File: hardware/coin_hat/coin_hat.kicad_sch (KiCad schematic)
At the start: 56 parts, among them J1 Pi 40-pin (bottom side), J10 Coin sensor, J11 Aux header, J12 Aux 12V switched, J2 Belt motor, J3 Feeder motor, J4 Diverter servo (1 SIG / 2 V+ 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, J5 12 V in 5.5/2.1, J6 LED ring (WS2812), J7 Key light 12V switched, J9 Home: feeder, Q1 AO3400, Q2 AO3400, Q3 AO3400, U1 Raspberry Pi Pico, U2 StepStick (TMC2209 or A4988), U3 StepStick (TMC2209 or A4988), U5 12V->5V 5A module (Pololu D24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, U6 74AHCT1G125, U7 CAT24C32, U8 12V->5-6V 3A servo buck (Polo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

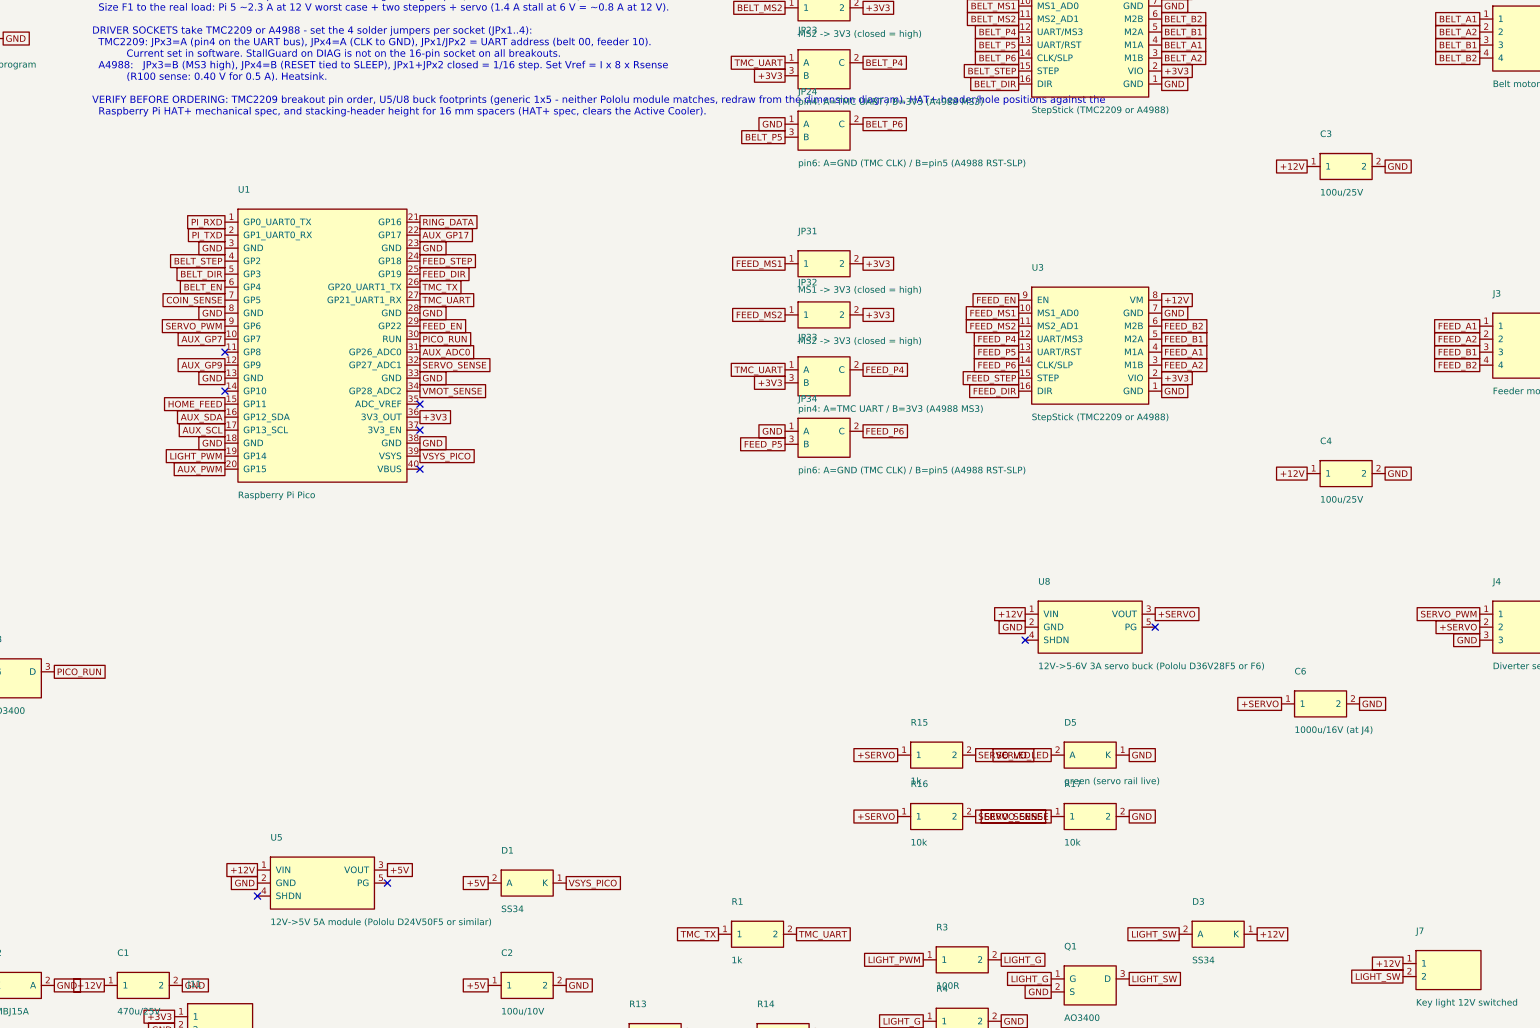
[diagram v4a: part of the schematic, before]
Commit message: coin_hat: draw Pololu buck footprints from the drill guides
U5 and U8 were a generic 1x5 header that matched neither module. Add a
project footprint library (coin_hat.pretty + fp-lib-table) with
Pololu_D24V50F5 and Pololu_D36V28Fx, placing pads and #2 mounting holes
at the coordinates in Pololu's drill-guide DXFs (reg15d01, reg24g), top
view, pad 1 = EN:

  D24V50F5  EN VIN GND GND VOUT
  D36V28Fx  EN VIN GND GND VOUT, PG 0.1" inboard of EN

Replace the generic Buck symbol with one symbol per module. EN is left
open (100k pull-up to VIN on both modules) and PG is unused. ERC is
clean, every pin maps to a pad, and the floor plan still packs with the
real 18.4 x 20.9 courtyards.

Co-Authored-By: Claude Opus 5.5 <noreply@anthropic.com>
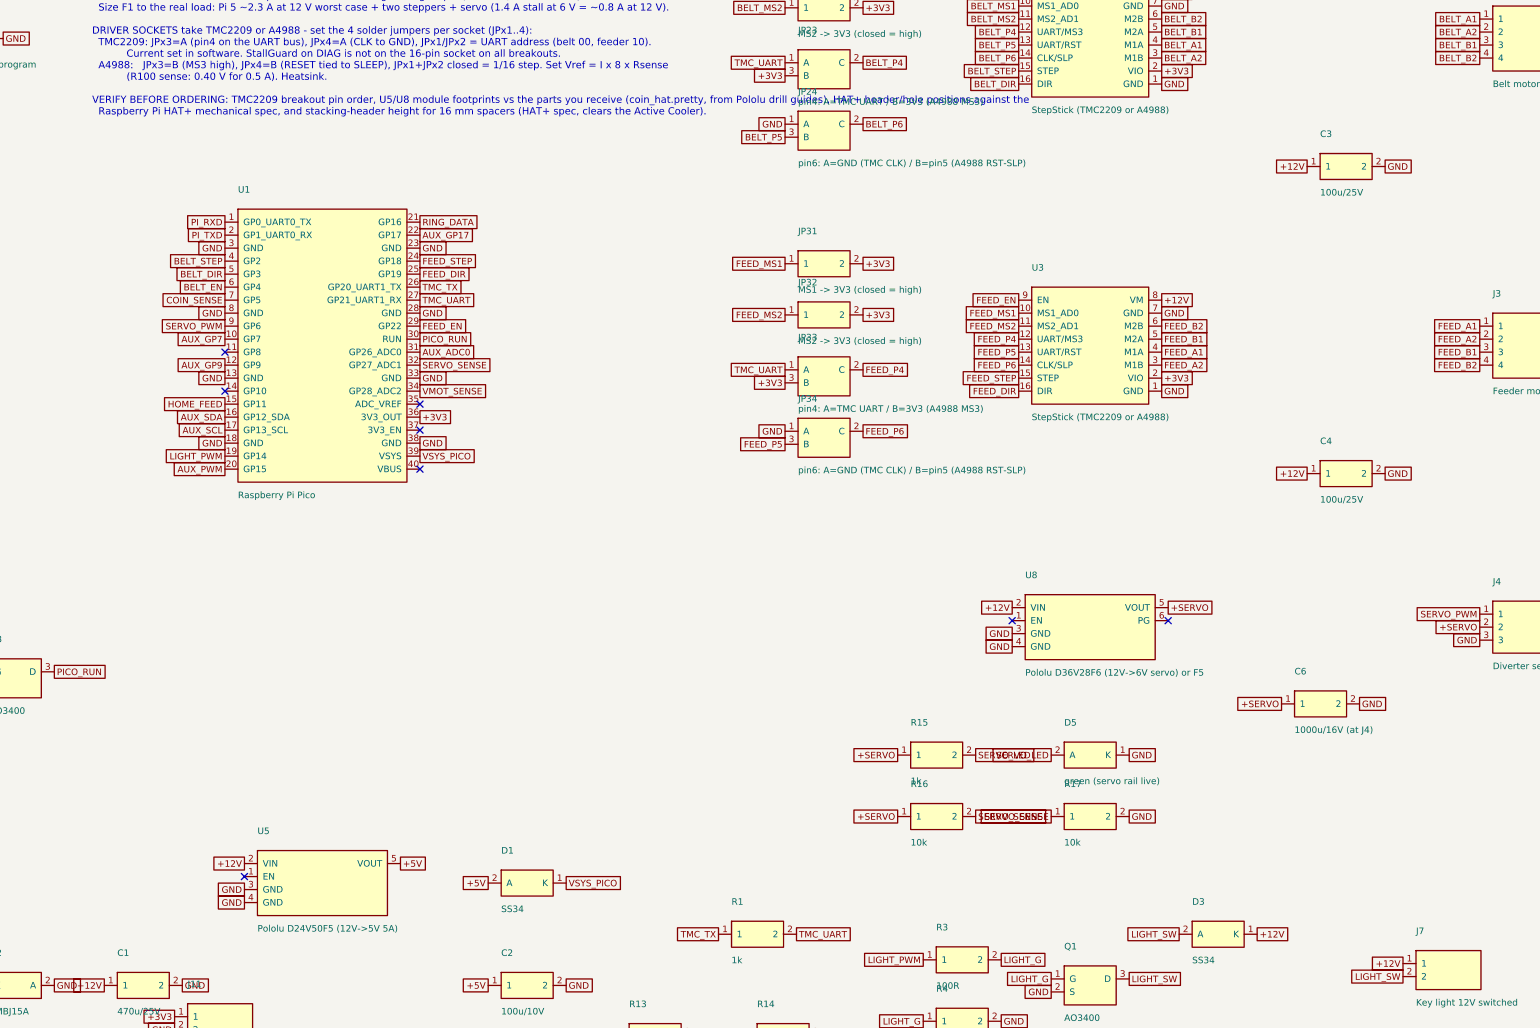
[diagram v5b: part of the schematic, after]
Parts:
- removed U5: 12V->5V 5A module (Pololu D24V50F5 or similar), Connector_PinHeader_2.54mm:PinHeader_1x05_P2.54mm_Vertical, symbol coin_hat:Buck
- removed U8: 12V->5-6V 3A servo buck (Pololu D36V28F5 or F6), Connector_PinHeader_2.54mm:PinHeader_1x05_P2.54mm_Vertical, symbol coin_hat:Buck
- added U5: Pololu D24V50F5 (12V->5V 5A), coin_hat:Pololu_D24V50F5, symbol coin_hat:D24V50F5
- added U8: Pololu D36V28F6 (12V->6V servo) or F5, coin_hat:Pololu_D36V28Fx, symbol coin_hat:D36V28Fx
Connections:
- net +12V: now also U5.2 (VIN), U8.2 (VIN)
- net +5V: now also U5.5 (VOUT)
- net +SERVO: now also U8.5 (VOUT)
- net GND: now also U5.3 (GND), U5.4 (GND), U8.3 (GND), U8.4 (GND)
- no-connect marks 33 -> 32

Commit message: coin_hat: update PCB from schematic and place all footprints
Pull all 56 footprints into the board with their nets and symbol links
(so a GUI Update PCB matches them instead of duplicating), and place
them on the checked floor plan: J1 on the bottom with pin 1 at the
HAT+ position (8.37, 4.77), Pico with USB toward the open +x side,
connectors, fuse and jack on the overhang end.

DRC fixes along the way: move the left-end column up so the jack's
switch pin clears the 0.5 mm edge rule, tighten the two overhang-end
corners to 1 mm so J2/J5 don't overhang the radius, move edge-clipped
reference labels onto their parts, and mark the solder jumpers
not-in-BOM to match their footprints.

DRC: 0 errors, 0 schematic-parity issues, no courtyard overlaps; only
unrouted nets and silkscreen overlaps remain. Ignore *.kicad_prl
(per-user view state).

Co-Authored-By: Claude Opus 5.5 <noreply@anthropic.com>
Claude-Session: https://claude.ai/code/session_01EPngbBgcoS7WRgtdrApT7C
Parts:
- JP1, JP21, JP22, JP23, JP24, JP31, JP32, JP33, JP34: now left out of the parts list
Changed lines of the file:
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@@
   )
   (symbol (lib_id "coin_hat:Jumper") (at 248 34 0) (unit 1)
-    (exclude_from_sim no) (in_bom yes) (on_board yes) (dnp no)
+    (exclude_from_sim no) (in_bom no) (on_board yes) (dnp no)
     (property "Reference" "JP21" (at 242.92 27.65 0) (effects (font (size 1.27 1.27)) (justify left)))
     (property "Value" "MS1 -> 3V3 (closed = high)" (at 242.92 39.08 0) (effects (font (size 1.27 1.27)) (justify left)))
@@
   )
   (symbol (lib_id "coin_hat:Jumper") (at 248 44 0) (unit 1)
-    (exclude_from_sim no) (in_bom yes) (on_board yes) (dnp no)
+    (exclude_from_sim no) (in_bom no) (on_board yes) (dnp no)
     (property "Reference" "JP22" (at 242.92 37.65 0) (effects (font (size 1.27 1.27)) (justify left)))
     (property "Value" "MS2 -> 3V3 (closed = high)" (at 242.92 49.08 0) (effects (font (size 1.27 1.27)) (justify left)))
@@
   )
   (symbol (lib_id "coin_hat:Jumper3") (at 248 56 0) (unit 1)
-    (exclude_from_sim no) (in_bom yes) (on_board yes) (dnp no)
+    (exclude_from_sim no) (in_bom no) (on_board yes) (dnp no)
     (property "Reference" "JP23" (at 242.92 48.38 0) (effects (font (size 1.27 1.27)) (justify left)))
     (property "Value" "pin4: A=TMC UART / B=3V3 (A4988 MS3)" (at 242.92 62.35 0) (effects (font (size 1.27 1.27)) (justify left)))
@@
   )
   (symbol (lib_id "coin_hat:Jumper3") (at 248 68 0) (unit 1)
-    (exclude_from_sim no) (in_bom yes) (on_board yes) (dnp no)
+    (exclude_from_sim no) (in_bom no) (on_board yes) (dnp no)
     (property "Reference" "JP24" (at 242.92 60.38 0) (effects (font (size 1.27 1.27)) (justify left)))
     (property "Value" "pin6: A=GND (TMC CLK) / B=pin5 (A4988 RST-SLP)" (at 242.92 74.35 0) (effects (font (size 1.27 1.27)) (justify left)))
@@
   )
   (symbol (lib_id "coin_hat:Jumper") (at 248 94 0) (unit 1)
-    (exclude_from_sim no) (in_bom yes) (on_board yes) (dnp no)
+    (exclude_from_sim no) (in_bom no) (on_board yes) (dnp no)
     (property "Reference" "JP31" (at 242.92 87.65 0) (effects (font (size 1.27 1.27)) (justify left)))
     (property "Value" "MS1 -> 3V3 (closed = high)" (at 242.92 99.08 0) (effects (font (size 1.27 1.27)) (justify left)))
@@
   )
   (symbol (lib_id "coin_hat:Jumper") (at 248 104 0) (unit 1)
-    (exclude_from_sim no) (in_bom yes) (on_board yes) (dnp no)
+    (exclude_from_sim no) (in_bom no) (on_board yes) (dnp no)
     (property "Reference" "JP32" (at 242.92 97.65 0) (effects (font (size 1.27 1.27)) (justify left)))
     (property "Value" "MS2 -> 3V3 (closed = high)" (at 242.92 109.08 0) (effects (font (size 1.27 1.27)) (justify left)))
@@
   )
   (symbol (lib_id "coin_hat:Jumper3") (at 248 116 0) (unit 1)
-    (exclude_from_sim no) (in_bom yes) (on_board yes) (dnp no)
+    (exclude_from_sim no) (in_bom no) (on_board yes) (dnp no)
     (property "Reference" "JP33" (at 242.92 108.38 0) (effects (font (size 1.27 1.27)) (justify left)))
     (property "Value" "pin4: A=TMC UART / B=3V3 (A4988 MS3)" (at 242.92 122.35 0) (effects (font (size 1.27 1.27)) (justify left)))
@@
   )
   (symbol (lib_id "coin_hat:Jumper3") (at 248 128 0) (unit 1)
-    (exclude_from_sim no) (in_bom yes) (on_board yes) (dnp no)
+    (exclude_from_sim no) (in_bom no) (on_board yes) (dnp no)
     (property "Reference" "JP34" (at 242.92 120.38 0) (effects (font (size 1.27 1.27)) (justify left)))
     (property "Value" "pin6: A=GND (TMC CLK) / B=pin5 (A4988 RST-SLP)" (at 242.92 134.35 0) (effects (font (size 1.27 1.27)) (justify left)))
@@
   )
   (symbol (lib_id "coin_hat:Jumper") (at 80 50 0) (unit 1)
-    (exclude_from_sim no) (in_bom yes) (on_board yes) (dnp no)
+    (exclude_from_sim no) (in_bom no) (on_board yes) (dnp no)
     (property "Reference" "JP1" (at 74.92 43.65 0) (effects (font (size 1.27 1.27)) (justify left)))
     (property "Value" "WP->GND to program" (at 74.92 55.08 0) (effects (font (size 1.27 1.27)) (justify left)))

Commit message: coin_hat: route the board and generate JLCPCB / PCBWay files
Fully routed 2-layer board, KiCad 9 DRC clean (0 violations, 0
unconnected, 0 schematic-parity issues). Freerouting did the bulk; the
Pi 5V feed to J1 pins 2/4 is hand-placed and locked (1.5 mm, necking to
1.0 mm past the mounting hole). Net classes for high-current, power,
motor and ground nets, GND poured on both layers, and copper keepouts
under the HAT+ standoffs (3.1 mm bottom, 2.6 mm top).

Placement changes to make it route: driver column 1 mm right, Pico and
its neighbours 1.5 mm down, gate resistors spread out. J5 becomes the
CUI PJ-102AH footprint (same pad pattern, 5 A rated).

Schematic symbols now carry LCSC / Manufacturer / MPN fields (JLCPCB
basic parts where available). make_fab.py writes fab/: a Gerber + drill
zip, JLCPCB BOM + CPL (SMD only, rotation corrections applied) and a
PCBWay BOM + centroid.

Co-Authored-By: Claude Opus 5.5 <noreply@anthropic.com>
Claude-Session: https://claude.ai/code/session_01EPngbBgcoS7WRgtdrApT7C
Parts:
- D1, D3, D4: LCSC (none) -> C8678; MPN (none) -> SS34; Manufacturer (none) -> MDD
- D2: LCSC (none) -> C19077569; MPN (none) -> SMBJ15A
- D5: LCSC (none) -> C965804; MPN (none) -> XL-1608UGC-04; Manufacturer (none) -> XINGLIGHT
- F1: MPN (none) -> 3568 holder + 4 A mini blade fuse; Manufacturer (none) -> Keystone
- J10, J6: LCSC (none) -> C144394; MPN (none) -> B3B-XH-A(LF)(SN); Manufacturer (none) -> JST
- J12, J7, J9: LCSC (none) -> C158012; MPN (none) -> B2B-XH-A(LF)(SN); Manufacturer (none) -> JST
- J2, J3: LCSC (none) -> C144395; MPN (none) -> B4B-XH-A(LF)(SN); Manufacturer (none) -> JST
- J5: value 12 V in 5.5/2.1 -> 12 V in 5.5/2.1 (CUI PJ-102AH, 5 A); footprint Connector_BarrelJack:BarrelJack_Horizontal -> Connector_BarrelJack:BarrelJack_CUI_PJ-102AH_Horizontal; LCSC (none) -> C3096093; MPN (none) -> PJ-102AH; Manufacturer (none) -> CUI Devices
- Q1, Q2, Q3: LCSC (none) -> C20917; MPN (none) -> AO3400A; Manufacturer (none) -> Alpha & Omega
- R1, R15, R8: LCSC (none) -> C21190; MPN (none) -> 0603WAF1001T5E; Manufacturer (none) -> UNI-ROYAL
- R10, R11: LCSC (none) -> C23018; MPN (none) -> 0603WAF3901T5E; Manufacturer (none) -> UNI-ROYAL
- R12, R13: LCSC (none) -> C25803; MPN (none) -> 0603WAF1003T5E; Manufacturer (none) -> UNI-ROYAL
- R14: LCSC (none) -> C22809; MPN (none) -> 0603WAF1502T5E; Manufacturer (none) -> UNI-ROYAL
- R16, R17, R4, R6, R9: LCSC (none) -> C25804; MPN (none) -> 0603WAF1002T5E; Manufacturer (none) -> UNI-ROYAL
- R3, R5: LCSC (none) -> C22775; MPN (none) -> 0603WAF1000T5E; Manufacturer (none) -> UNI-ROYAL
- U1: MPN (none) -> Raspberry Pi Pico (SC0915); Manufacturer (none) -> Raspberry Pi
- U5: MPN (none) -> D24V50F5 (#2851); Manufacturer (none) -> Pololu
- U6: LCSC (none) -> C350557; MPN (none) -> SN74AHCT1G125DCKR; Manufacturer (none) -> Texas Instruments
- U7: value CAT24C32 -> M24C32-RMN6TP; LCSC (none) -> C79920; MPN (none) -> M24C32-RMN6TP; Manufacturer (none) -> STMicroelectronics
- U8: MPN (none) -> D36V28F6 (#3783); Manufacturer (none) -> Pololu

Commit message: coin_hat: pre-fab review fixes
- Move the Pico so its micro-USB socket is at the board edge; 9 mm of
  board sat in the footprint's USB-cable keepout and would have blocked
  the plug used for REPL / mpremote.
- Add 100 nF bypass caps C7 (U6 level shifter) and C8 (U7 HAT+ EEPROM),
  JLCPCB basic part C14663.
- Power-net vias 1.2/0.6 mm (~3 A); the switched outputs and the TVS
  each went through a single 0.4 mm via. One AUX_SW via stays 0.8/0.4
  for clearance, so J12 is rated ~1.5 A.
- Remove paste from the Pico pads (not fab-assembled).
- Move the EEPROM group into the pocket left of the Pico; the board now
  routes completely.

KiCad 9: ERC 0 errors, DRC 0 errors / 0 unconnected / 0 parity issues
(the Pico "differs from library" warning is the paste change). fab/
regenerated. README notes the J1 socket height needed for 16 mm
spacers, 12 V-only powering, and the jumper label order.

Co-Authored-By: Claude Opus 5.5 <noreply@anthropic.com>
Claude-Session: https://claude.ai/code/session_01EPngbBgcoS7WRgtdrApT7C
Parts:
- added C7: 100n (U6 bypass), Capacitor_SMD:C_0603_1608Metric, symbol coin_hat:Cap
- added C8: 100n (U7 bypass), Capacitor_SMD:C_0603_1608Metric, symbol coin_hat:Cap
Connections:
- net +5V: now also C7.1
- net GND: now also C7.2, C8.2
- net PI_3V3: now also C8.1
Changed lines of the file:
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@@
   )
   (no_connect (at 315.24 163.73))
+  (symbol (lib_id "coin_hat:Cap") (at 110 285 0) (unit 1)
+    (exclude_from_sim no) (in_bom yes) (on_board yes) (dnp no)
+    (property "Reference" "C7" (at 104.92 278.65 0) (effects (font (size 1.27 1.27)) (justify left)))
+    (property "Value" "100n (U6 bypass)" (at 104.92 290.08 0) (effects (font (size 1.27 1.27)) (justify left)))
+    (property "Footprint" "Capacitor_SMD:C_0603_1608Metric" (at 110 285 0) (effects (font (size 1.27 1.27)) (hide yes)))
+    (property "Datasheet" "" (at 110 285 0) (effects (font (size 1.27 1.27)) (hide yes)))
+    (property "LCSC" "C14663" (at 110 285 0) (effects (font (size 1.27 1.27)) (hide yes)))
+    (property "Manufacturer" "YAGEO" (at 110 285 0) (effects (font (size 1.27 1.27)) (hide yes)))
+    (property "MPN" "CC0603KRX7R9BB104" (at 110 285 0) (effects (font (size 1.27 1.27)) (hide yes)))
+    (pin "1")
+    (pin "2")
+    (instances (project "coin_hat" (path "/530641cf-7157-4f9d-b975-f11274705971" (reference "C7") (unit 1))))
+  )
+  (global_label "+5V" (shape passive) (at 102.38 285 180) (fields_autoplaced yes)
+    (effects (font (size 1.27 1.27)) (justify right))
+    (property "Intersheetrefs" "${INTERSHEET_REFS}" (at 102.38 285 0) (effects (font (size 1.27 1.27)) (hide yes)))
+  )
+  (global_label "GND" (shape passive) (at 117.62 285 0) (fields_autoplaced yes)
+    (effects (font (size 1.27 1.27)) (justify left))
+    (property "Intersheetrefs" "${INTERSHEET_REFS}" (at 117.62 285 0) (effects (font (size 1.27 1.27)) (hide yes)))
+  )
+  (symbol (lib_id "coin_hat:Cap") (at 45 50 0) (unit 1)
+    (exclude_from_sim no) (in_bom yes) (on_board yes) (dnp no)
+    (property "Reference" "C8" (at 39.92 43.65 0) (effects (font (size 1.27 1.27)) (justify left)))
+    (property "Value" "100n (U7 bypass)" (at 39.92 55.08 0) (effects (font (size 1.27 1.27)) (justify left)))
+    (property "Footprint" "Capacitor_SMD:C_0603_1608Metric" (at 45 50 0) (effects (font (size 1.27 1.27)) (hide yes)))
+    (property "Datasheet" "" (at 45 50 0) (effects (font (size 1.27 1.27)) (hide yes)))
+    (property "LCSC" "C14663" (at 45 50 0) (effects (font (size 1.27 1.27)) (hide yes)))
+    (property "Manufacturer" "YAGEO" (at 45 50 0) (effects (font (size 1.27 1.27)) (hide yes)))
+    (property "MPN" "CC0603KRX7R9BB104" (at 45 50 0) (effects (font (size 1.27 1.27)) (hide yes)))
+    (pin "1")
+    (pin "2")
+    (instances (project "coin_hat" (path "/530641cf-7157-4f9d-b975-f11274705971" (reference "C8") (unit 1))))
+  )
+  (global_label "PI_3V3" (shape passive) (at 37.38 50 180) (fields_autoplaced yes)
+    (effects (font (size 1.27 1.27)) (justify right))
+    (property "Intersheetrefs" "${INTERSHEET_REFS}" (at 37.38 50 0) (effects (font (size 1.27 1.27)) (hide yes)))
+  )
+  (global_label "GND" (shape passive) (at 52.62 50 0) (fields_autoplaced yes)
+    (effects (font (size 1.27 1.27)) (justify left))
+    (property "Intersheetrefs" "${INTERSHEET_REFS}" (at 52.62 50 0) (effects (font (size 1.27 1.27)) (hide yes)))
+  )
   (sheet_instances (path "/" (page "1")))
 )
